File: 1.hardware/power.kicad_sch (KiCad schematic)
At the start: 74 parts, among them IC1 LMR51610XDBVR, J1 12V~48V BAT_XT60_MALE, J2 12V-48V Jack

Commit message: 중간 저장
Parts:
- added C9: 47uF/100V, Capacitor_SMD:C_Elec_10x10.2, symbol Device:C_Polarized_Small_US
- C8: renamed from C7; value 100uF/100V -> 47uF/100V; footprint Capacitor_THT:CP_Radial_Tantal_D8.0mm_P5.00mm -> Capacitor_SMD:C_Elec_10x10.2
- renumbered C9 to C10, C10 to C11, C11 to C12, C12 to C13, C13 to C14, C14 to C15, C15 to C16, C16 to C17, C17 to C18, C18 to C19, C19 to C20, C20 to C21, C21 to C22, C22 to C23, C23 to C24, C24 to C25, C25 to C26, C26 to C27, C27 to C28, C28 to C29, C5 to C3, C3 to C4, C6 to C5, C4 to C6, C8 to C7, S5 to S1, TP3 to TP2, TP2 to TP3
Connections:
- net GNDPWR: now also C9.2
- net PWR_INPUT(12V~48V): now also C9.1
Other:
- moved on the sheet: C10, C11, C8

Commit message: 중간 저장
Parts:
- removed C12, C18: 22uF/10V, Capacitor_SMD:C_0603_1608Metric, symbol Device:C_Small_US
- removed C13, C19: 10uF/25V, Capacitor_SMD:C_0603_1608Metric, symbol Device:C_Small_US
- removed C24, C27: 0.1uF/50V, Capacitor_SMD:C_0603_1608Metric, symbol Device:C_Small_US
- removed D5: B5819WS, SamacSys_Parts_Project:SOD2613X100N, symbol SamacSys_Parts:B5819WS
- removed L6: MPL2016S2R2MHT, SamacSys_Parts_Project:INDC2116X100N, symbol SamacSys_Parts:MPL2016S2R2MHT
- removed PS1: TPS563201DDCT, SamacSys_Parts_Project:SOT95P280X110-6N, symbol SamacSys_Parts:TPS563201DDCT
- removed R10: 10k/0.1w, Resistor_SMD:R_0603_1608Metric, symbol Device:R_Small_US
- removed R6: 10k/0.063w, Resistor_SMD:R_0402_1005Metric, symbol Device:R_Small_US
- removed R9: 13.7k/0.1w, Resistor_SMD:R_0603_1608Metric, symbol Device:R_Small_US
- removed TP4: TP_1V8, TestPoint:TestPoint_Pad_D1.5mm, symbol Connector:TestPoint
- added C126, C128: 1uF/16V, Capacitor_SMD:C_0603_1608Metric, symbol Device:C_Small_US
- added IC11: TLV74018PDBVR, SamacSys_Parts_Project:SOT95P280X145-5N, symbol SamacSys_Parts:TLV74018PDBVR
- L7: value MPL2016S2R2MHT -> MPL2520S2R2MHT; footprint SamacSys_Parts_Project:INDC2116X100N -> Inductor_SMD:L_1008_2520Metric
- L8: value MPL2016S3R3MHT -> MPL2520S2R2MHT; footprint SamacSys_Parts_Project:INDC2116X100N -> Inductor_SMD:L_1008_2520Metric
- R4: value 30k/0.1w -> 20k/0.1w
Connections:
- net 1V8: now also C128.1, IC11.5 (OUT)
- net 5V: now also C126.1, IC11.1 (IN), IC11.3 (EN)
- net GND: now also C126.2, C128.2, IC11.2 (GND)
- net GNDPWR: now also J1.1 (Pin_1); no longer J1.2 (Pin_2)
- net at D2.2 (A): now also J1.2 (Pin_2); no longer J1.1 (Pin_1)
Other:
- note removed: "1.8V"
- moved on the sheet: J1

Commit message: 중간 저장
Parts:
- removed C2: 2.2uF/100V, Capacitor_SMD:C_Elec_6.3x5.4, symbol Device:C_Polarized_Small_US
- removed C20, C22: 22uF/10V, Capacitor_SMD:C_0603_1608Metric, symbol Device:C_Small_US
- removed C3, C5: 22uF/25V, Capacitor_SMD:C_Elec_5x5.8, symbol Device:C_Polarized_Small_US
- removed C7: 10uF/25V, Capacitor_SMD:C_Elec_4x5.4, symbol Device:C_Polarized_Small_US
- added C12: 10uF/50V, Capacitor_SMD:C_1206_3216Metric, symbol Device:C_Small_US
- added C13, C3, C5, C7: 22uF/25V, Capacitor_SMD:C_1206_3216Metric, symbol Device:C_Small_US
- added C18: 2.2uF/100V, Capacitor_SMD:C_1210_3225Metric, symbol Device:C_Small_US
- C14, C16: value 22uF/10V -> 22uF/25V; footprint Capacitor_SMD:C_0603_1608Metric -> Capacitor_SMD:C_1206_3216Metric
- C15, C17, C21, C23: value 10uF/25V -> 10uF/50V; footprint Capacitor_SMD:C_0603_1608Metric -> Capacitor_SMD:C_1206_3216Metric
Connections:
- net 12V: now also C12.1, C3.1, C7.1
- net 3V3: now also C13.1, C5.1; no longer C14.1
- net 5V: now also C14.1
- net GND: now also C12.2, C13.2, C18.2, C3.2, C5.2, C7.2
- net PWR_INPUT(12V~48V): now also C18.1

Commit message: 중간 저장
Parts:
- renumbered C6 to C1, C13 to C10, C28 to C11, C15 to C12, C21 to C13, C25 to C14, C7 to C15, C3 to C16, C12 to C17, C1 to C18, C14 to C19, C8 to C2, C16 to C20, C29 to C21, C18 to C22, C17 to C23, C23 to C24, C26 to C25, C9 to C3, C10 to C4, C11 to C5, C126 to C6, C128 to C7, C4 to C8, C5 to C9, D3 to D2, D2 to D3, D6 to D5, D7 to D6, IC11 to IC1, IC1 to IC2, J2 to J1, J1 to J2, L2 to L1, L7 to L2, L1 to L3, L3 to L4, L8 to L5, L4 to L6, L5 to L7, PS2 to PS1, PS3 to PS2, R3 to R1, R14 to R10, R8 to R11, R4 to R2, R5 to R3, R11 to R4, R12 to R5, R7 to R6, R1 to R7, R2 to R8, R13 to R9, TP3 to TP2, TP5 to TP3, TP2 to TP4, TP6 to TP5
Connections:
- net GND: now also R3.1
- net GNDPWR: no longer R3.1

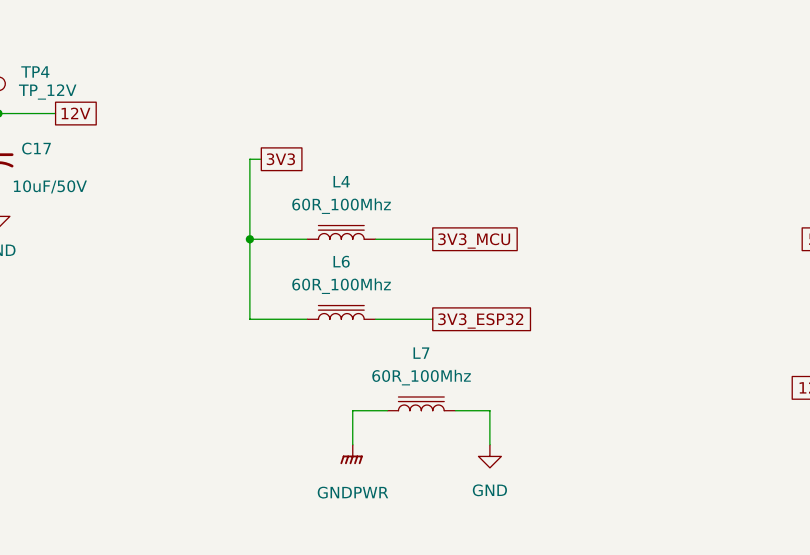
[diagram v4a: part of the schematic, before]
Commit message: 많이 간소화함 일부 핀이 비연결로 확인됨
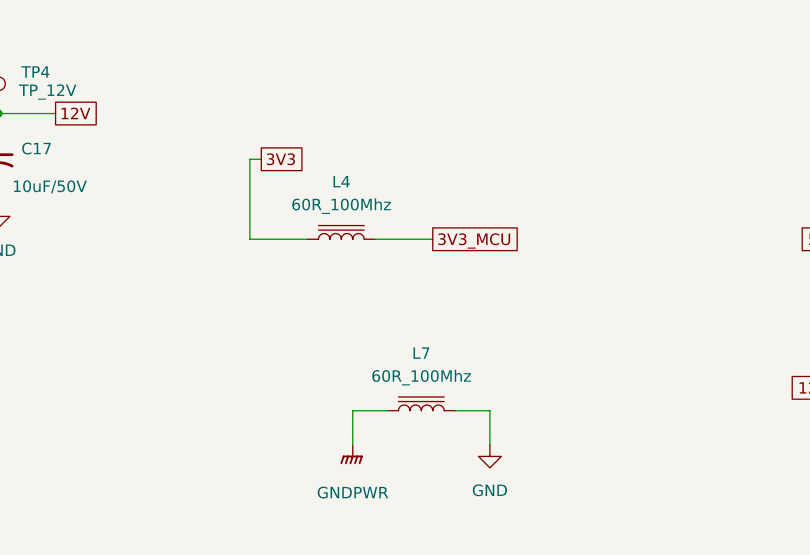
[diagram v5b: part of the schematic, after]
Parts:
- removed L6: 60R_100Mhz, Inductor_SMD:L_0603_1608Metric, symbol Device:L_Iron
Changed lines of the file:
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@@
 	)
 	(junction
-		(at 152.4 118.11)
-		(diameter 0)
-		(color 0 0 0 0)
-	)
-	(junction
 		(at 320.04 134.62)
 		(diameter 0)
@@
 	(wire
 		(pts
-			(xy 158.75 127) (xy 152.4 127)
-		)
-		(stroke
-			(width 0)
-			(type default)
-		)
-	)
-	(wire
-		(pts
 			(xy 76.2 104.14) (xy 76.2 110.49)
 		)
@@
 	(wire
 		(pts
-			(xy 166.37 127) (xy 172.72 127)
-		)
-		(stroke
-			(width 0)
-			(type default)
-		)
-	)
-	(wire
-		(pts
 			(xy 278.13 73.66) (xy 308.61 73.66)
 		)
@@
 	(wire
 		(pts
-			(xy 152.4 118.11) (xy 152.4 127)
-		)
-		(stroke
-			(width 0)
-			(type default)
-		)
-	)
-	(wire
-		(pts
 			(xy 86.36 123.19) (xy 86.36 125.73)
 		)
@@
 		)
 	)
-	(global_label "3V3_ESP32"
-		(shape passive)
-		(at 172.72 127 0)
-		(fields_autoplaced yes)
-		(effects
-			(font
-				(size 1.27 1.27)
-			)
-			(justify left)
-		)
-		(property "Intersheetrefs" "${INTERSHEET_REFS}"
-			(at 185.1166 127 0)
-			(effects
-				(font
-					(size 1.27 1.27)
-				)
-				(justify left)
-				(hide yes)
-			)
-		)
-	)
 	(global_label "12V"
 		(shape passive)
@@
 					(unit 1)
 				)
-			)
-		)
-	)
-	(symbol
-		(lib_id "Device:L_Iron")
-		(at 162.56 127 90)
-		(unit 1)
-		(exclude_from_sim no)
-		(in_bom yes)
-		(on_board yes)
-		(dnp no)
-		(fields_autoplaced yes)
-		(property "Reference" "L6"
-			(at 162.56 120.65 90)
-			(effects
-				(font
-					(size 1.27 1.27)
-				)
-			)
-		)
-		(property "Value" "60R_100Mhz"
-			(at 162.56 123.19 90)
-			(effects
-				(font
-					(size 1.27 1.27)
-				)
-			)
-		)
-		(property "Footprint" "Inductor_SMD:L_0603_1608Metric"
-			(at 162.56 127 0)
-			(effects
-				(font
-					(size 1.27 1.27)
-				)
-				(hide yes)
-			)
-		)
-		(property "Datasheet" "~"
-			(at 162.56 127 0)
-			(effects
-				(font
-					(size 1.27 1.27)
-				)
-				(hide yes)
-			)
-		)
-		(property "Description" "Inductor with iron core"
-			(at 162.56 127 0)
-			(effects
-				(font
-					(size 1.27 1.27)
-				)
-				(hide yes)
-			)
-		)
-		(pin "1"
-		)
-		(pin "2"
-		)
-		(instances
-			(project "bldc_motor_controller"
-				(path "/a25adab6-a8c3-4e0e-8ba9-baac00aaa394/fa552ebf-4859-4df7-97cc-cc5957e0d3a3"
-					(reference "L6")
-					(unit 1)
-				)

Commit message: 오류 일단 다 잡음
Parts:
- C21, C25: footprint Capacitor_SMD:C_0603_1608Metric -> Capacitor_SMD:C_0402_1005Metric
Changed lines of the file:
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@@
 			)
 		)
-		(property "Footprint" "Capacitor_SMD:C_0603_1608Metric"
+		(property "Footprint" "Capacitor_SMD:C_0402_1005Metric"
 			(at 265.43 139.7 0)
 			(effects
@@
 			)
 		)
-		(property "Footprint" "Capacitor_SMD:C_0603_1608Metric"
+		(property "Footprint" "Capacitor_SMD:C_0402_1005Metric"
 			(at 308.61 123.19 0)
 			(effects

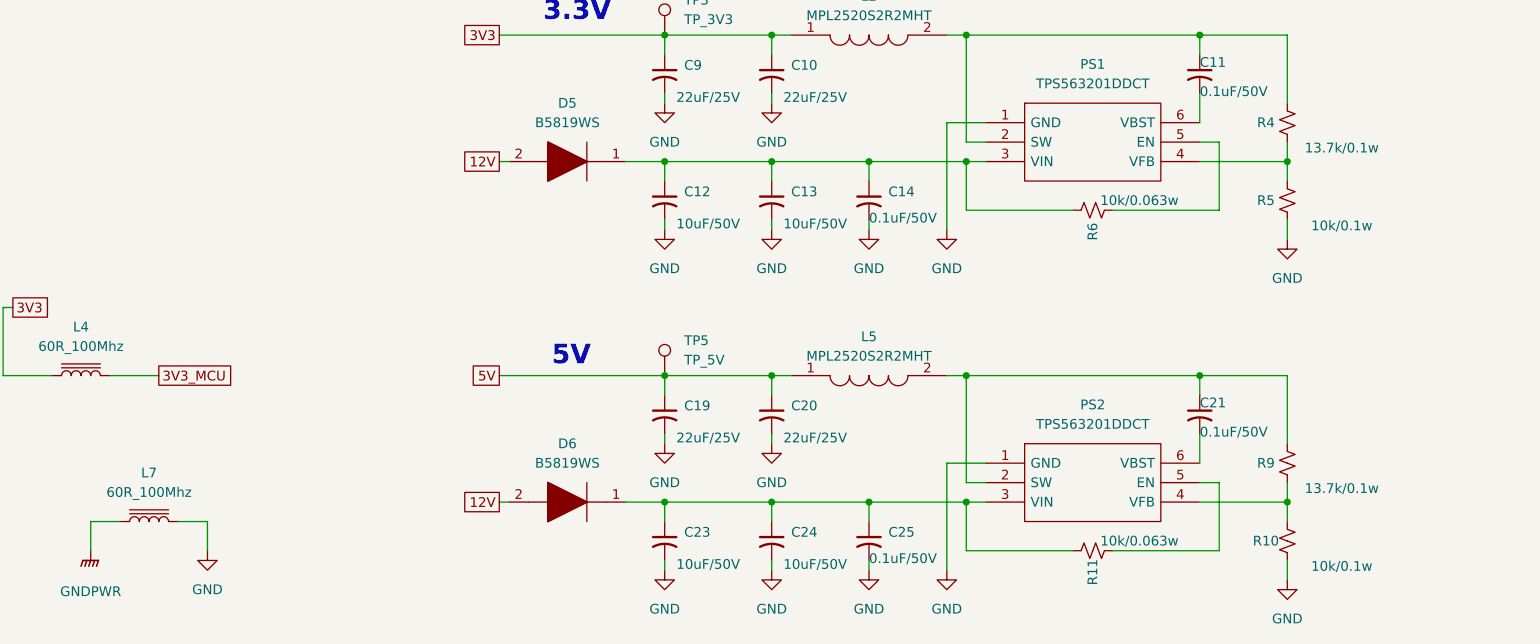
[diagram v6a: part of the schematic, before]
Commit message: 부품 통일 및 필터 부분 캡 선정등 필요해보임
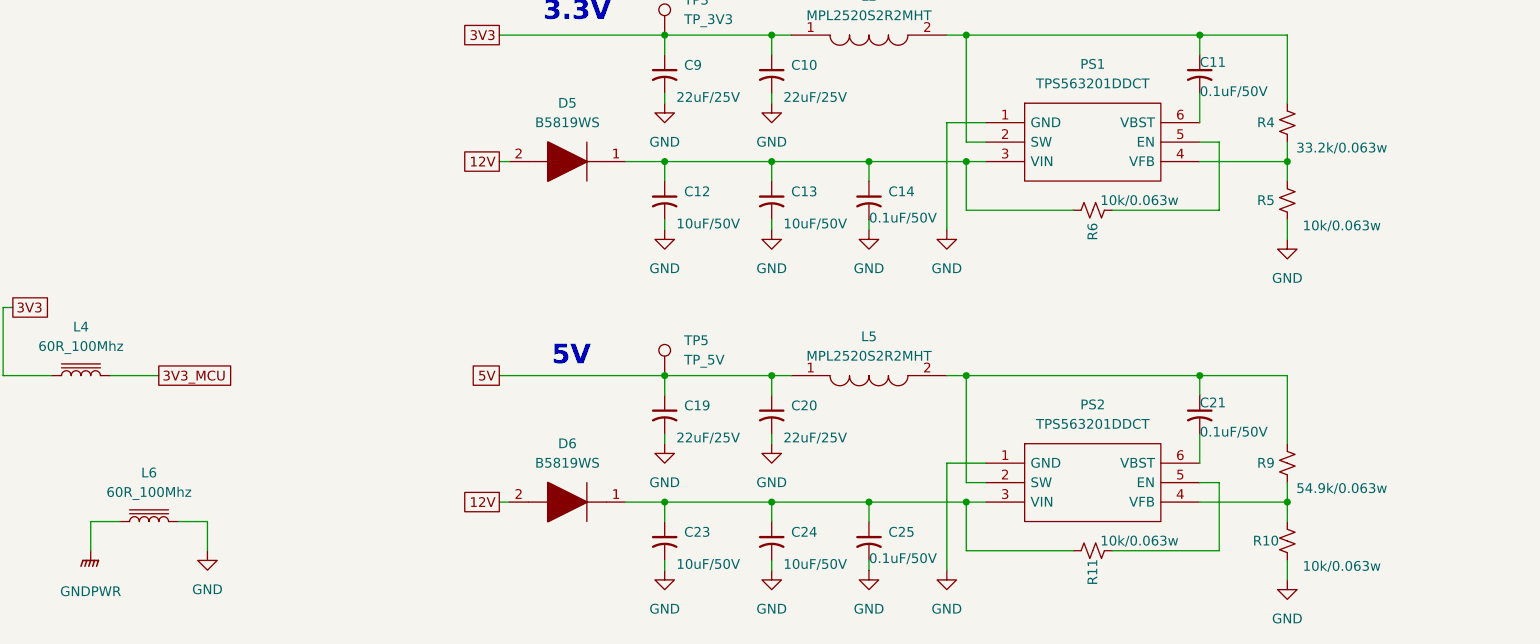
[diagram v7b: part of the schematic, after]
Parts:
- C11, C14: footprint Capacitor_SMD:C_0603_1608Metric -> Capacitor_SMD:C_0402_1005Metric
- R10, R5: value 10k/0.1w -> 10k/0.063w
- R4: value 13.7k/0.1w -> 33.2k/0.063w
- R9: value 13.7k/0.1w -> 54.9k/0.063w
- TP1, TP3, TP4, TP5: now left out of the parts list
- renumbered L7 to L6
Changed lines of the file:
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@@
 			)
 		)
-		(property "Value" "10k/0.1w"
+		(property "Value" "10k/0.063w"
 			(at 327.152 143.002 0)
 			(effects
@@
 			)
 		)
-		(property "Footprint" "Capacitor_SMD:C_0603_1608Metric"
+		(property "Footprint" "Capacitor_SMD:C_0402_1005Metric"
 			(at 265.43 95.25 0)
 			(effects
@@
 		(unit 1)
 		(exclude_from_sim no)
-		(in_bom yes)
+		(in_bom no)
 		(on_board yes)
 		(dnp no)
@@
 		(unit 1)
 		(exclude_from_sim no)
-		(in_bom yes)
+		(in_bom no)
 		(on_board yes)
 		(dnp no)
@@
 		(unit 1)
 		(exclude_from_sim no)
-		(in_bom yes)
+		(in_bom no)
 		(on_board yes)
 		(dnp no)
@@
 		(dnp no)
 		(fields_autoplaced yes)
-		(property "Reference" "L7"
+		(property "Reference" "L6"
 			(at 171.45 130.81 90)
 			(effects
@@
 			(project "bldc_motor_controller"
 				(path "/a25adab6-a8c3-4e0e-8ba9-baac00aaa394/fa552ebf-4859-4df7-97cc-cc5957e0d3a3"
-					(reference "L7")
+					(reference "L6")
 					(unit 1)
 				)
@@
 		(unit 1)
 		(exclude_from_sim no)
-		(in_bom yes)
+		(in_bom no)
 		(on_board yes)
 		(dnp no)
@@
 			)
 		)
-		(property "Value" "13.7k/0.1w"
+		(property "Value" "54.9k/0.063w"
 			(at 327.152 132.842 0)
 			(effects
@@
 			)
 		)
-		(property "Value" "13.7k/0.1w"
+		(property "Value" "33.2k/0.063w"
 			(at 327.152 88.392 0)
 			(effects
@@
 			)
 		)
-		(property "Value" "10k/0.1w"
+		(property "Value" "10k/0.063w"
 			(at 327.152 98.552 0)
 			(effects
@@
 			)
 		)
-		(property "Footprint" "Capacitor_SMD:C_0603_1608Metric"
+		(property "Footprint" "Capacitor_SMD:C_0402_1005Metric"
 			(at 308.61 78.74 0)
 			(effects

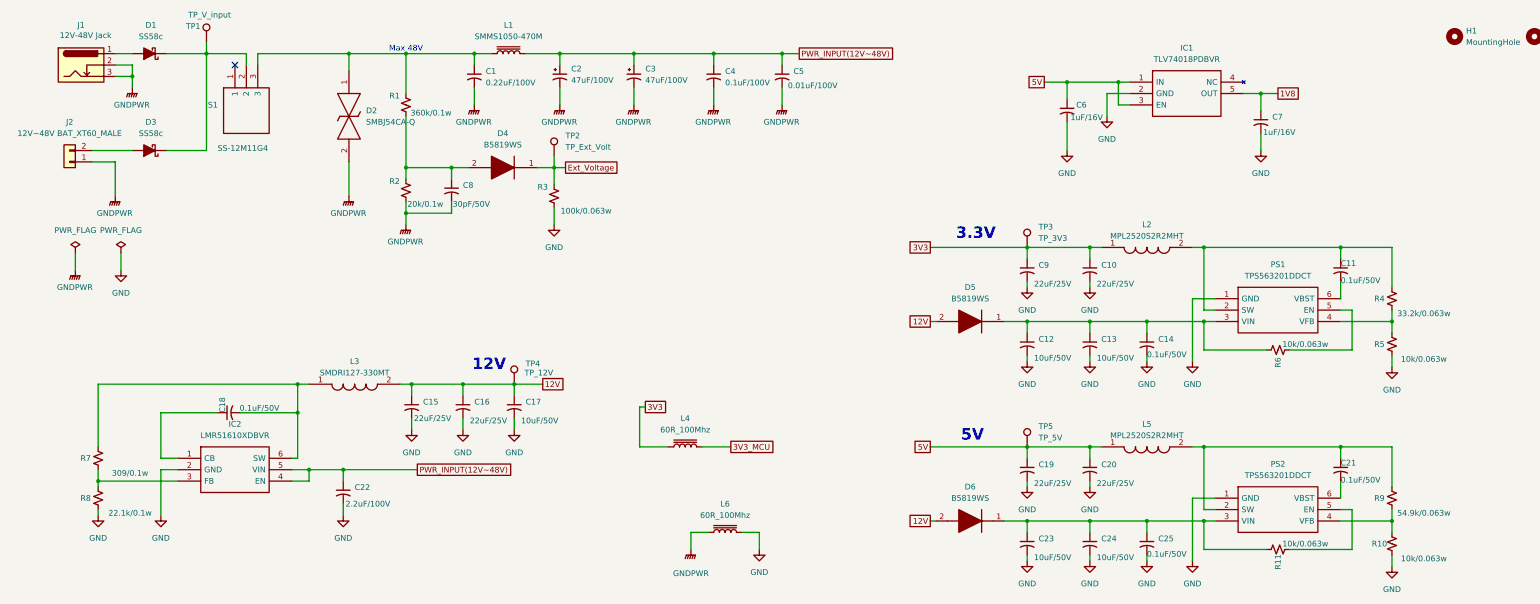
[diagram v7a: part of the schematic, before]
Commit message: 거의 완성 근데 JLC에서 포지션이 좀 개판임
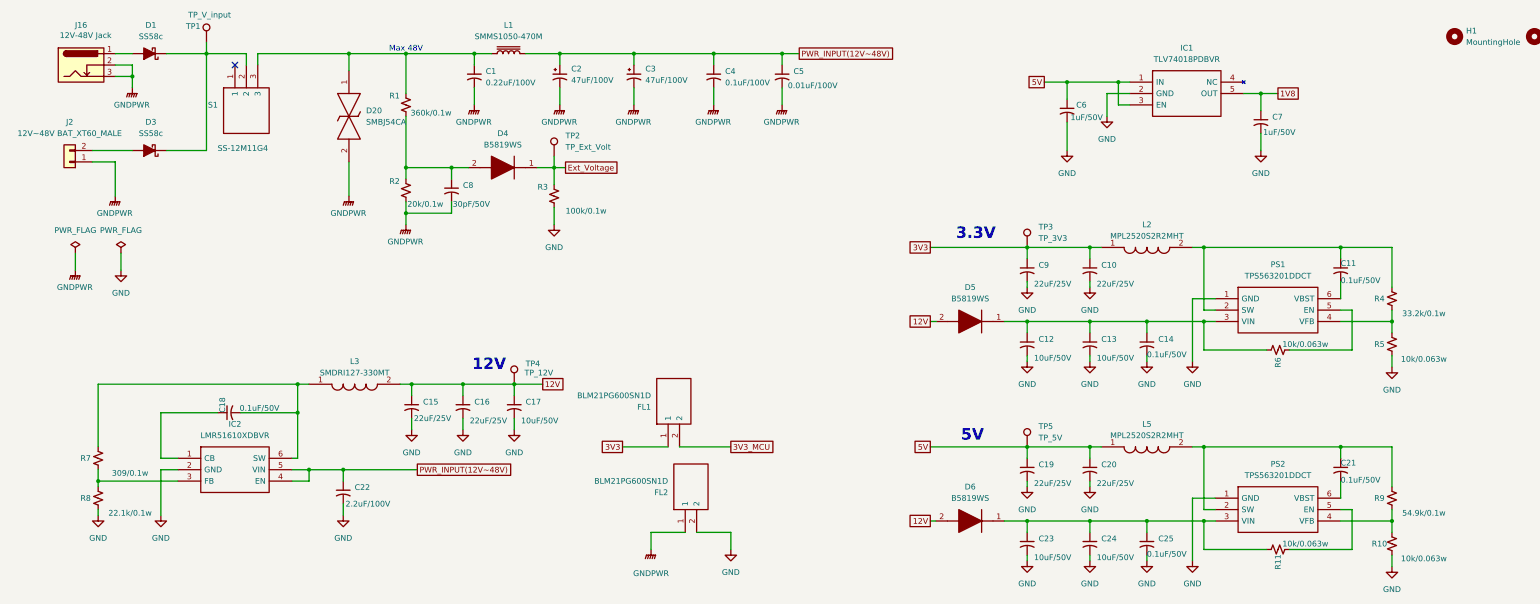
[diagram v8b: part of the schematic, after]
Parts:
- removed D2: SMBJ54CA-Q, SamacSys_Parts_Project:DIOM5436X244N, symbol SamacSys_Parts:SMBJ54CA-Q
- removed J1: 12V-48V Jack, Connector_BarrelJack:BarrelJack_Wuerth_6941xx301002, symbol Connector:Barrel_Jack_Switch_Pin3Ring
- removed L4, L6: 60R_100Mhz, Inductor_SMD:L_0603_1608Metric, symbol Device:L_Iron
- added D20: SMBJ54CA, SamacSys_Parts_Project:DIONM5436X261N, symbol SamacSys_Parts:SMBJ54CA
- added FL1, FL2: BLM21PG600SN1D, SamacSys_Parts_Project:BLM21AG102BH1J, symbol SamacSys_Parts:BLM21PG600SN1D
- added J16: 12V-48V Jack, Library:DC-S009A-D025-7A, symbol Connector:Barrel_Jack_Switch_Pin3Ring
- C4, C5: footprint Capacitor_SMD:C_0402_1005Metric -> Capacitor_SMD:C_0603_1608Metric
- C6, C7: value 1uF/16V -> 1uF/50V
- R10, R5: footprint Resistor_SMD:R_0603_1608Metric -> Resistor_SMD:R_0402_1005Metric
- R3: value 100k/0.063w -> 100k/0.1w; footprint Resistor_SMD:R_0402_1005Metric -> Resistor_SMD:R_0603_1608Metric
- R4: value 33.2k/0.063w -> 33.2k/0.1w
- R9: value 54.9k/0.063w -> 54.9k/0.1w
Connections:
- net 3V3: now also FL1.1
- net 3V3_MCU: now also FL1.2
- net GND: now also FL2.2
- net GNDPWR: now also D20.2, FL2.1, J16.2, J16.3
- net at C1.1, L1.1, R1.2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: now also D20.1
- net at D1.2 (A): now also J16.1
